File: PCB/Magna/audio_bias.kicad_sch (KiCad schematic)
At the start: 5 parts, among them U1101 NE5532

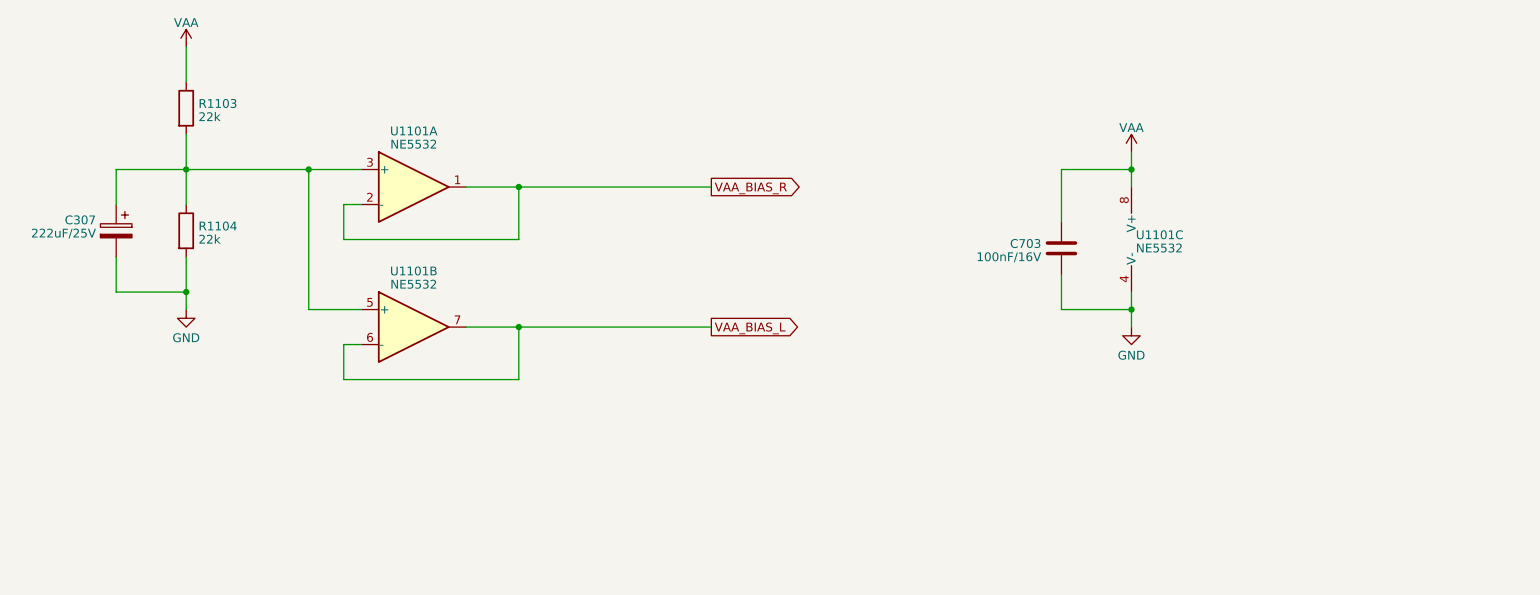
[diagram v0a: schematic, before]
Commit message: Update analogue frontend and add potentiometer interface
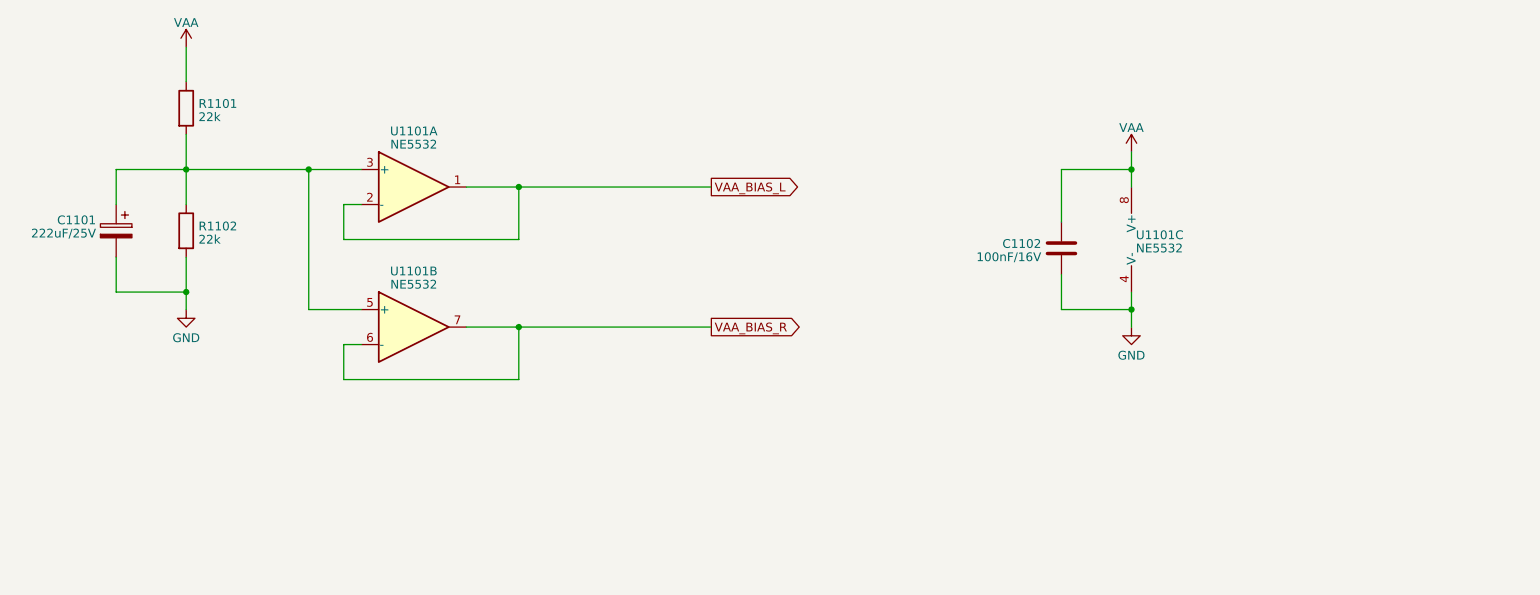
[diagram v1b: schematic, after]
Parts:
- renumbered C307 to C1101, C703 to C1102, R1103 to R1101, R1104 to R1102
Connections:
- net VAA_BIAS_L: now also U1101.1, U1101.2 (-); no longer U1101.6 (-), U1101.7
- net VAA_BIAS_R: now also U1101.6 (-), U1101.7; no longer U1101.1, U1101.2 (-)
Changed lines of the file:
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@@
     (stroke (width 0) (type default))
   )
-  (global_label "VAA_BIAS_L" (shape output) (at 127 73.66 0) (fields_autoplaced)
+  (global_label "VAA_BIAS_L" (shape output) (at 127 53.34 0) (fields_autoplaced)
     (effects (font (size 1.27 1.27)) (justify left))
-    (property "Intersheetrefs" "${INTERSHEET_REFS}" (at 140.3078 73.66 0)
+    (property "Intersheetrefs" "${INTERSHEET_REFS}" (at 140.3078 53.34 0)
       (effects (font (size 1.27 1.27)) (justify left) hide)
     )
   )
-  (global_label "VAA_BIAS_R" (shape output) (at 127 53.34 0) (fields_autoplaced)
+  (global_label "VAA_BIAS_R" (shape output) (at 127 73.66 0) (fields_autoplaced)
     (effects (font (size 1.27 1.27)) (justify left))
-    (property "Intersheetrefs" "${INTERSHEET_REFS}" (at 140.5497 53.34 0)
+    (property "Intersheetrefs" "${INTERSHEET_REFS}" (at 140.5497 73.66 0)
       (effects (font (size 1.27 1.27)) (justify left) hide)
     )
@@
   (symbol (lib_id "power:VAA") (at 50.8 33.02 0) (unit 1)
     (in_bom yes) (on_board yes) (dnp no) (fields_autoplaced)
-    (property "Reference" "#PWR01103" (at 50.8 36.83 0)
+    (property "Reference" "#PWR01101" (at 50.8 36.83 0)
       (effects (font (size 1.27 1.27)) hide)
     )
@@
       (project "Magna"
         (path "/1469ea1f-a157-49dc-a369-2d42fa17695d/22259812-9e7f-4230-9f2b-a9eb5ce4aaf1/eddc896c-2eca-4cc9-a7eb-0b3af1aefe11"
+          (reference "#PWR01101") (unit 1)
+        )
+      )
+    )
+  )
+  (symbol (lib_id "power:GND") (at 50.8 71.12 0) (unit 1)
+    (in_bom yes) (on_board yes) (dnp no) (fields_autoplaced)
+    (property "Reference" "#PWR01102" (at 50.8 77.47 0)
+      (effects (font (size 1.27 1.27)) hide)
+    )
+    (property "Value" "GND" (at 50.8 75.2555 0)
+      (effects (font (size 1.27 1.27)))
+    )
+    (property "Footprint" "" (at 50.8 71.12 0)
+      (effects (font (size 1.27 1.27)) hide)
+    )
+    (property "Datasheet" "" (at 50.8 71.12 0)
+      (effects (font (size 1.27 1.27)) hide)
+    )
+    (pin "1")
+    (instances
+      (project "Magna"
+        (path "/1469ea1f-a157-49dc-a369-2d42fa17695d/22259812-9e7f-4230-9f2b-a9eb5ce4aaf1/eddc896c-2eca-4cc9-a7eb-0b3af1aefe11"
+          (reference "#PWR01102") (unit 1)
+        )
+      )
+    )
+  )
+  (symbol (lib_id "power:VAA") (at 187.96 48.26 0) (unit 1)
+    (in_bom yes) (on_board yes) (dnp no) (fields_autoplaced)
+    (property "Reference" "#PWR01103" (at 187.96 52.07 0)
+      (effects (font (size 1.27 1.27)) hide)
+    )
+    (property "Value" "VAA" (at 187.96 44.7581 0)
+      (effects (font (size 1.27 1.27)))
+    )
+    (property "Footprint" "" (at 187.96 48.26 0)
+      (effects (font (size 1.27 1.27)) hide)
+    )
+    (property "Datasheet" "" (at 187.96 48.26 0)
+      (effects (font (size 1.27 1.27)) hide)
+    )
+    (pin "1")
+    (instances
+      (project "Magna"
+        (path "/1469ea1f-a157-49dc-a369-2d42fa17695d/22259812-9e7f-4230-9f2b-a9eb5ce4aaf1/eddc896c-2eca-4cc9-a7eb-0b3af1aefe11"
           (reference "#PWR01103") (unit 1)
         )
@@
     )
   )
-  (symbol (lib_id "power:GND") (at 50.8 71.12 0) (unit 1)
-    (in_bom yes) (on_board yes) (dnp no) (fields_autoplaced)
-    (property "Reference" "#PWR01104" (at 50.8 77.47 0)
-      (effects (font (size 1.27 1.27)) hide)
-    )
-    (property "Value" "GND" (at 50.8 75.2555 0)
-      (effects (font (size 1.27 1.27)))
-    )
-    (property "Footprint" "" (at 50.8 71.12 0)
-      (effects (font (size 1.27 1.27)) hide)
-    )
-    (property "Datasheet" "" (at 50.8 71.12 0)
-      (effects (font (size 1.27 1.27)) hide)
-    )
-    (pin "1")
-    (instances
-      (project "Magna"
-        (path "/1469ea1f-a157-49dc-a369-2d42fa17695d/22259812-9e7f-4230-9f2b-a9eb5ce4aaf1/eddc896c-2eca-4cc9-a7eb-0b3af1aefe11"
-          (reference "#PWR01104") (unit 1)
-        )
-      )
-    )
-  )
-  (symbol (lib_id "power:VAA") (at 187.96 48.26 0) (unit 1)
-    (in_bom yes) (on_board yes) (dnp no) (fields_autoplaced)
-    (property "Reference" "#PWR01102" (at 187.96 52.07 0)
-      (effects (font (size 1.27 1.27)) hide)
-    )
-    (property "Value" "VAA" (at 187.96 44.7581 0)
-      (effects (font (size 1.27 1.27)))
-    )
-    (property "Footprint" "" (at 187.96 48.26 0)
-      (effects (font (size 1.27 1.27)) hide)
-    )
-    (property "Datasheet" "" (at 187.96 48.26 0)
-      (effects (font (size 1.27 1.27)) hide)
-    )
-    (pin "1")
-    (instances
-      (project "Magna"
-        (path "/1469ea1f-a157-49dc-a369-2d42fa17695d/22259812-9e7f-4230-9f2b-a9eb5ce4aaf1/eddc896c-2eca-4cc9-a7eb-0b3af1aefe11"
-          (reference "#PWR01102") (unit 1)
-        )
-      )
-    )
-  )
   (symbol (lib_id "Device:R") (at 50.8 41.91 0) (unit 1)
     (in_bom yes) (on_board yes) (dnp no) (fields_autoplaced)
-    (property "Reference" "R1103" (at 52.578 41.2663 0)
+    (property "Reference" "R1101" (at 52.578 41.2663 0)
       (effects (font (size 1.27 1.27)) (justify left))
     )
@@
       (project "Magna"
         (path "/1469ea1f-a157-49dc-a369-2d42fa17695d/22259812-9e7f-4230-9f2b-a9eb5ce4aaf1/eddc896c-2eca-4cc9-a7eb-0b3af1aefe11"
-          (reference "R1103") (unit 1)
+          (reference "R1101") (unit 1)
         )
       )
@@
   (symbol (lib_id "Device:R") (at 50.8 59.69 0) (unit 1)
     (in_bom yes) (on_board yes) (dnp no) (fields_autoplaced)
-    (property "Reference" "R1104" (at 52.578 59.0463 0)
+    (property "Reference" "R1102" (at 52.578 59.0463 0)
       (effects (font (size 1.27 1.27)) (justify left))
     )
@@
       (project "Magna"
         (path "/1469ea1f-a157-49dc-a369-2d42fa17695d/22259812-9e7f-4230-9f2b-a9eb5ce4aaf1/eddc896c-2eca-4cc9-a7eb-0b3af1aefe11"
-          (reference "R1104") (unit 1)
+          (reference "R1102") (unit 1)
         )
       )
@@
   (symbol (lib_id "Device:C_Polarized") (at 40.64 59.69 0) (mirror y) (unit 1)
     (in_bom yes) (on_board yes) (dnp no)
-    (property "Reference" "C307" (at 37.719 58.1573 0)
+    (property "Reference" "C1101" (at 37.719 58.1573 0)
       (effects (font (size 1.27 1.27)) (justify left))
     )
@@
     (instances
       (project "Magna"
-        (path "/1469ea1f-a157-49dc-a369-2d42fa17695d/22259812-9e7f-4230-9f2b-a9eb5ce4aaf1/beaa37c2-0104-4021-8685-9eb18db04351"
-          (reference "C307") (unit 1)
-        )
-        (path "/1469ea1f-a157-49dc-a369-2d42fa17695d/22259812-9e7f-4230-9f2b-a9eb5ce4aaf1/63203deb-a3d6-4c27-a099-379311360062"
-          (reference "C407") (unit 1)
-        )
-        (path "/1469ea1f-a157-49dc-a369-2d42fa17695d/22259812-9e7f-4230-9f2b-a9eb5ce4aaf1/eddc896c-2eca-4cc9-a7eb-0b3af1aefe11"
-          (reference "C1102") (unit 1)
+        (path "/1469ea1f-a157-49dc-a369-2d42fa17695d/22259812-9e7f-4230-9f2b-a9eb5ce4aaf1/eddc896c-2eca-4cc9-a7eb-0b3af1aefe11"
+          (reference "C1101") (unit 1)
         )
       )
@@
   (symbol (lib_id "Device:C") (at 177.8 62.23 0) (mirror y) (unit 1)
     (in_bom yes) (on_board yes) (dnp no)
-    (property "Reference" "C703" (at 174.879 61.5863 0)
+    (property "Reference" "C1102" (at 174.879 61.5863 0)
       (effects (font (size 1.27 1.27)) (justify left))
     )
@@
     (instances
       (project "Magna"
-        (path "/1469ea1f-a157-49dc-a369-2d42fa17695d/46a2120f-089e-4436-ab6c-5e02739b600f"
-          (reference "C703") (unit 1)
-        )
-        (path "/1469ea1f-a157-49dc-a369-2d42fa17695d/22259812-9e7f-4230-9f2b-a9eb5ce4aaf1/beaa37c2-0104-4021-8685-9eb18db04351"
-          (reference "C301") (unit 1)
-        )
-        (path "/1469ea1f-a157-49dc-a369-2d42fa17695d/22259812-9e7f-4230-9f2b-a9eb5ce4aaf1/63203deb-a3d6-4c27-a099-379311360062"
-          (reference "C401") (unit 1)
-        )
-        (path "/1469ea1f-a157-49dc-a369-2d42fa17695d/22259812-9e7f-4230-9f2b-a9eb5ce4aaf1/0f70dfcf-faa8-4745-8ffb-98640ceeb78a"
-          (reference "C508") (unit 1)
-        )
-        (path "/1469ea1f-a157-49dc-a369-2d42fa17695d/22259812-9e7f-4230-9f2b-a9eb5ce4aaf1/396242ef-243f-440f-bcad-6ad240970fd6"
-          (reference "C608") (unit 1)
-        )
-        (path "/1469ea1f-a157-49dc-a369-2d42fa17695d/22259812-9e7f-4230-9f2b-a9eb5ce4aaf1/eddc896c-2eca-4cc9-a7eb-0b3af1aefe11"
-          (reference "C1101") (unit 1)
+        (path "/1469ea1f-a157-49dc-a369-2d42fa17695d/22259812-9e7f-4230-9f2b-a9eb5ce4aaf1/eddc896c-2eca-4cc9-a7eb-0b3af1aefe11"
+          (reference "C1102") (unit 1)
         )
       )
@@
   (symbol (lib_id "power:GND") (at 187.96 73.66 0) (unit 1)
     (in_bom yes) (on_board yes) (dnp no) (fields_autoplaced)
-    (property "Reference" "#PWR01101" (at 187.96 80.01 0)
+    (property "Reference" "#PWR01104" (at 187.96 80.01 0)
       (effects (font (size 1.27 1.27)) hide)
     )
@@
       (project "Magna"
         (path "/1469ea1f-a157-49dc-a369-2d42fa17695d/22259812-9e7f-4230-9f2b-a9eb5ce4aaf1/eddc896c-2eca-4cc9-a7eb-0b3af1aefe11"
-          (reference "#PWR01101") (unit 1)
-        )
-      )
+          (reference "#PWR01104") (unit 1)
+        )
+      )

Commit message: Add final touched to all schematics
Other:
- moved on the sheet: C1101, C1102, R1101, R1102, U1101A, U1101B, U1101C

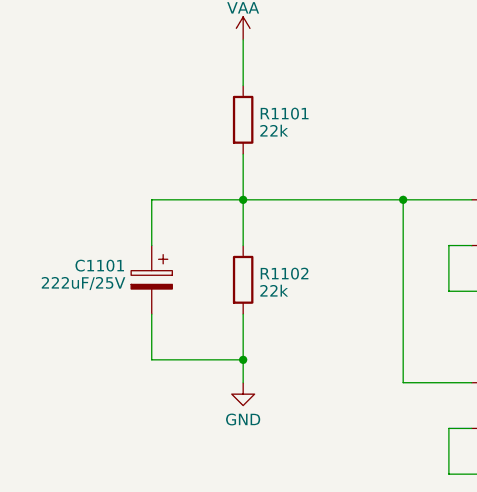
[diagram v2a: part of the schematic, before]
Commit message: Update capacitors to parts in JLC library
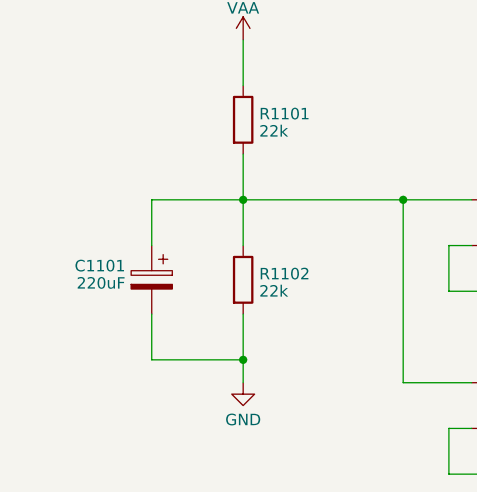
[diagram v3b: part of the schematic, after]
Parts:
- C1101: value 222uF/25V -> 220uF; footprint Capacitor_SMD:CP_Elec_8x10 -> Capacitor_SMD:CP_Elec_4x5.8; LCSC C340762 -> C2165067
- C1102: footprint Capacitor_SMD:C_0402_1005Metric -> Capacitor_SMD:C_0805_2012Metric; LCSC C1525 -> C218638
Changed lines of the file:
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@@
       (effects (font (size 1.27 1.27)) (justify left))
     )
-    (property "Value" "222uF/25V" (at 56.769 89.2883 0)
+    (property "Value" "220uF" (at 56.769 89.2883 0)
       (effects (font (size 1.27 1.27)) (justify left))
     )
-    (property "Footprint" "Capacitor_SMD:CP_Elec_8x10" (at 58.7248 92.71 0)
+    (property "Footprint" "Capacitor_SMD:CP_Elec_4x5.8" (at 58.7248 92.71 0)
       (effects (font (size 1.27 1.27)) hide)
     )
@@
       (effects (font (size 1.27 1.27)) hide)
     )
-    (property "LCSC" "C340762" (at 59.69 88.9 90)
+    (property "LCSC" "C2165067" (at 59.69 88.9 90)
       (effects (font (size 1.27 1.27)) hide)
     )
@@
       (effects (font (size 1.27 1.27)) (justify left))
     )
-    (property "Footprint" "Capacitor_SMD:C_0402_1005Metric" (at 225.0948 96.52 0)
+    (property "Footprint" "Capacitor_SMD:C_0805_2012Metric" (at 225.0948 96.52 0)
       (effects (font (size 1.27 1.27)) hide)
     )
@@
       (effects (font (size 1.27 1.27)) hide)
     )
-    (property "LCSC" "C1525" (at 226.06 92.71 0)
+    (property "LCSC" "C218638" (at 226.06 92.71 0)
       (effects (font (size 1.27 1.27)) hide)
     )

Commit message: Select parts for all components
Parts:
- R1101, R1102: footprint (none) -> Resistor_SMD:R_0805_2012Metric; LCSC (none) -> C479095
- U1101: LCSC (none) -> C7426
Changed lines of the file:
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@@
       (effects (font (size 1.27 1.27)) (justify left))
     )
-    (property "Footprint" "" (at 68.072 71.12 90)
+    (property "Footprint" "Resistor_SMD:R_0805_2012Metric" (at 68.072 71.12 90)
       (effects (font (size 1.27 1.27)) hide)
     )
     (property "Datasheet" "~" (at 69.85 71.12 0)
+      (effects (font (size 1.27 1.27)) hide)
+    )
+    (property "LCSC" "C479095" (at 69.85 71.12 0)
       (effects (font (size 1.27 1.27)) hide)
     )
@@
     )
     (property "Datasheet" "http://www.ti.com/lit/ds/symlink/ne5532.pdf" (at 102.87 102.87 0)
+      (effects (font (size 1.27 1.27)) hide)
+    )
+    (property "LCSC" "C7426" (at 102.87 102.87 0)
       (effects (font (size 1.27 1.27)) hide)
     )
@@
       (effects (font (size 1.27 1.27)) hide)
     )
+    (property "LCSC" "C7426" (at 238.76 91.44 0)
+      (effects (font (size 1.27 1.27)) hide)
+    )
     (pin "1")
     (pin "2")
@@
       (effects (font (size 1.27 1.27)) hide)
     )
+    (property "LCSC" "C7426" (at 102.87 82.55 0)
+      (effects (font (size 1.27 1.27)) hide)
+    )
     (pin "1")
     (pin "2")
@@
       (effects (font (size 1.27 1.27)) (justify left))
     )
-    (property "Footprint" "" (at 68.072 88.9 90)
+    (property "Footprint" "Resistor_SMD:R_0805_2012Metric" (at 68.072 88.9 90)
       (effects (font (size 1.27 1.27)) hide)
     )
@@
       (effects (font (size 1.27 1.27)) hide)
     )
+    (property "LCSC" "C479095" (at 69.85 88.9 0)
+      (effects (font (size 1.27 1.27)) hide)
+    )

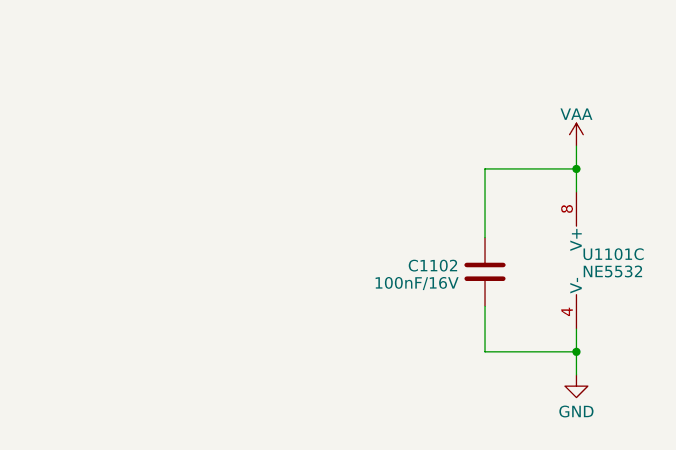
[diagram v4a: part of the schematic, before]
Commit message: Add even more component footprints and partnumbers
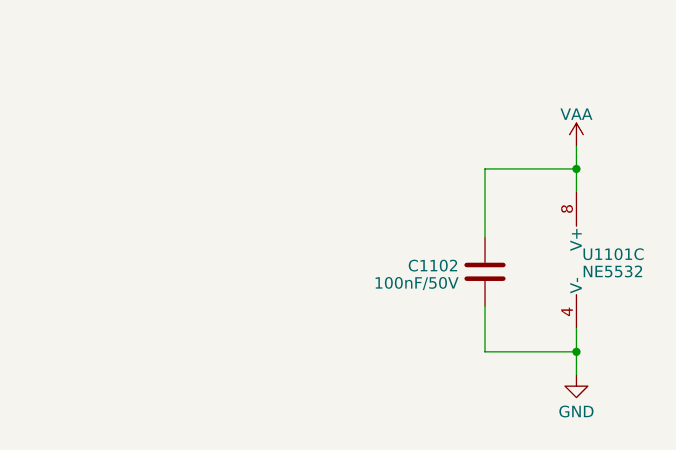
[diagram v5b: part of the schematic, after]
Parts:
- C1102: value 100nF/16V -> 100nF/50V; footprint Capacitor_SMD:C_0805_2012Metric -> Capacitor_SMD:C_0805_2012Metric_Pad1.18x1.45mm_HandSolder; LCSC C218638 -> C49678
- R1101, R1102: footprint Resistor_SMD:R_0805_2012Metric -> Resistor_SMD:R_0805_2012Metric_Pad1.20x1.40mm_HandSolder
- U1101: footprint (none) -> Package_SO:SOIC-8_3.9x4.9mm_P1.27mm
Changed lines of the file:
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@@
       (effects (font (size 1.27 1.27)) (justify left))
     )
-    (property "Footprint" "Resistor_SMD:R_0805_2012Metric" (at 68.072 71.12 90)
+    (property "Footprint" "Resistor_SMD:R_0805_2012Metric_Pad1.20x1.40mm_HandSolder" (at 68.072 71.12 90)
       (effects (font (size 1.27 1.27)) hide)
     )
@@
       (effects (font (size 1.27 1.27)))
     )
-    (property "Footprint" "" (at 102.87 102.87 0)
+    (property "Footprint" "Package_SO:SOIC-8_3.9x4.9mm_P1.27mm" (at 102.87 102.87 0)
       (effects (font (size 1.27 1.27)) hide)
     )
@@
       (effects (font (size 1.27 1.27)) (justify left))
     )
-    (property "Footprint" "" (at 238.76 91.44 0)
+    (property "Footprint" "Package_SO:SOIC-8_3.9x4.9mm_P1.27mm" (at 238.76 91.44 0)
       (effects (font (size 1.27 1.27)) hide)
     )
@@
       (effects (font (size 1.27 1.27)))
     )
-    (property "Footprint" "" (at 102.87 82.55 0)
+    (property "Footprint" "Package_SO:SOIC-8_3.9x4.9mm_P1.27mm" (at 102.87 82.55 0)
       (effects (font (size 1.27 1.27)) hide)
     )
@@
       (effects (font (size 1.27 1.27)) (justify left))
     )
-    (property "Footprint" "Resistor_SMD:R_0805_2012Metric" (at 68.072 88.9 90)
+    (property "Footprint" "Resistor_SMD:R_0805_2012Metric_Pad1.20x1.40mm_HandSolder" (at 68.072 88.9 90)
       (effects (font (size 1.27 1.27)) hide)
     )
@@
       (effects (font (size 1.27 1.27)) (justify left))
     )
-    (property "Value" "100nF/16V" (at 223.139 93.9873 0)
+    (property "Value" "100nF/50V" (at 223.139 93.9873 0)
       (effects (font (size 1.27 1.27)) (justify left))
     )
-    (property "Footprint" "Capacitor_SMD:C_0805_2012Metric" (at 225.0948 96.52 0)
+    (property "Footprint" "Capacitor_SMD:C_0805_2012Metric_Pad1.18x1.45mm_HandSolder" (at 225.0948 96.52 0)
       (effects (font (size 1.27 1.27)) hide)
     )
@@
       (effects (font (size 1.27 1.27)) hide)
     )
-    (property "LCSC" "C218638" (at 226.06 92.71 0)
+    (property "LCSC" "C49678" (at 226.06 92.71 0)
       (effects (font (size 1.27 1.27)) hide)
     )
